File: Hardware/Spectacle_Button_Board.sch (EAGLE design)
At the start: 50 parts, among them J17 AUDIO-JACK3, J19 FTDI_DEVICE, J20 AUDIO-JACK3, U1 CY8C4146LQI-S422, U2 3.3V/150mA

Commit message: Quick schematic changes, ready for QC review
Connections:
- net GND: now also J17.TIP, J20.TIP; no longer J17.RING2, J20.RING2
- net SCL: now also J17.RING2, J20.RING2; no longer J17.RING1, J20.RING1
- net SDA: now also J17.RING1, J20.RING1; no longer J17.TIP, J20.TIP
- net VIN: now also D5.2; no longer D5.1
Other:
- moved on the sheet: D4, J17, J20
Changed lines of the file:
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@@
 <?xml version="1.0" encoding="utf-8"?>
 <!DOCTYPE eagle SYSTEM "eagle.dtd">
-<eagle version="7.3.0">
+<eagle version="7.6.0">
 <drawing>
 <settings>
@@
 <instance part="C5" gate="G$1" x="17.78" y="109.22"/>
 <instance part="C6" gate="G$1" x="7.62" y="109.22"/>
-<instance part="GND9" gate="1" x="185.42" y="63.5"/>
+<instance part="GND9" gate="1" x="180.34" y="63.5"/>
 <instance part="SUPPLY7" gate="G$1" x="190.5" y="93.98"/>
 <instance part="R3" gate="G$1" x="198.12" y="83.82" rot="R90"/>
@@
 <instance part="R6" gate="G$1" x="226.06" y="162.56" rot="R180"/>
 <instance part="GND15" gate="1" x="38.1" y="132.08"/>
-<instance part="J17" gate="G$1" x="167.64" y="73.66"/>
-<instance part="D4" gate="G$1" x="208.28" y="58.42"/>
+<instance part="J17" gate="G$1" x="167.64" y="73.66" rot="MR180"/>
+<instance part="D4" gate="G$1" x="208.28" y="68.58" rot="MR180"/>
 <instance part="D5" gate="G$1" x="208.28" y="40.64"/>
 <instance part="D6" gate="G$1" x="60.96" y="63.5"/>
@@
 <instance part="SUPPLY13" gate="G$1" x="205.74" y="101.6"/>
 <instance part="SUPPLY14" gate="G$1" x="228.6" y="137.16"/>
-<instance part="J20" gate="G$1" x="167.64" y="53.34"/>
-<instance part="GND21" gate="1" x="185.42" y="43.18"/>
+<instance part="J20" gate="G$1" x="167.64" y="53.34" rot="MR180"/>
+<instance part="GND21" gate="1" x="180.34" y="43.18"/>
 <instance part="LOGO1" gate="G$1" x="127" y="15.24"/>
 <instance part="LOGO2" gate="G$1" x="50.8" y="0"/>
@@
 </segment>
 <segment>
-<pinref part="J17" gate="G$1" pin="RING2"/>
 <pinref part="GND9" gate="1" pin="GND"/>
-<wire x1="172.72" y1="68.58" x2="185.42" y2="68.58" width="0.1524" layer="91"/>
-<wire x1="185.42" y1="68.58" x2="185.42" y2="66.04" width="0.1524" layer="91"/>
+<pinref part="J17" gate="G$1" pin="TIP"/>
+<wire x1="172.72" y1="76.2" x2="180.34" y2="76.2" width="0.1524" layer="91"/>
+<wire x1="180.34" y1="76.2" x2="180.34" y2="66.04" width="0.1524" layer="91"/>
 </segment>
 <segment>
@@
 <wire x1="223.52" y1="45.72" x2="226.06" y2="45.72" width="0.1524" layer="91"/>
 <wire x1="226.06" y1="45.72" x2="226.06" y2="43.18" width="0.1524" layer="91"/>
-<wire x1="226.06" y1="45.72" x2="226.06" y2="63.5" width="0.1524" layer="91"/>
-<junction x="226.06" y="45.72"/>
 <pinref part="D4" gate="G$1" pin="3"/>
 <wire x1="226.06" y1="63.5" x2="223.52" y2="63.5" width="0.1524" layer="91"/>
-</segment>
-<segment>
-<pinref part="J20" gate="G$1" pin="RING2"/>
+<wire x1="226.06" y1="63.5" x2="226.06" y2="45.72" width="0.1524" layer="91"/>
+<junction x="226.06" y="45.72"/>
+</segment>
+<segment>
 <pinref part="GND21" gate="1" pin="GND"/>
-<wire x1="172.72" y1="48.26" x2="185.42" y2="48.26" width="0.1524" layer="91"/>
-<wire x1="185.42" y1="48.26" x2="185.42" y2="45.72" width="0.1524" layer="91"/>
+<pinref part="J20" gate="G$1" pin="TIP"/>
+<wire x1="172.72" y1="55.88" x2="180.34" y2="55.88" width="0.1524" layer="91"/>
+<wire x1="180.34" y1="55.88" x2="180.34" y2="45.72" width="0.1524" layer="91"/>
 </segment>
 </net>
@@
 </segment>
 <segment>
+<pinref part="D5" gate="G$1" pin="2"/>
 <pinref part="SUPPLY7" gate="G$1" pin="VIN"/>
+<wire x1="203.2" y1="43.18" x2="190.5" y2="43.18" width="0.1524" layer="91"/>
+<wire x1="190.5" y1="43.18" x2="190.5" y2="48.26" width="0.1524" layer="91"/>
+<pinref part="J20" gate="G$1" pin="EARTH"/>
+<wire x1="190.5" y1="48.26" x2="190.5" y2="68.58" width="0.1524" layer="91"/>
+<wire x1="190.5" y1="68.58" x2="190.5" y2="93.98" width="0.1524" layer="91"/>
+<wire x1="172.72" y1="48.26" x2="190.5" y2="48.26" width="0.1524" layer="91"/>
+<junction x="190.5" y="48.26"/>
 <pinref part="J17" gate="G$1" pin="EARTH"/>
-<wire x1="190.5" y1="78.74" x2="190.5" y2="93.98" width="0.1524" layer="91"/>
-<wire x1="172.72" y1="78.74" x2="190.5" y2="78.74" width="0.1524" layer="91"/>
-<wire x1="190.5" y1="78.74" x2="195.58" y2="78.74" width="0.1524" layer="91"/>
-<junction x="190.5" y="78.74"/>
-<wire x1="195.58" y1="78.74" x2="195.58" y2="58.42" width="0.1524" layer="91"/>
-<pinref part="D5" gate="G$1" pin="1"/>
-<wire x1="195.58" y1="58.42" x2="195.58" y2="48.26" width="0.1524" layer="91"/>
-<wire x1="195.58" y1="48.26" x2="203.2" y2="48.26" width="0.1524" layer="91"/>
-<pinref part="J20" gate="G$1" pin="EARTH"/>
-<wire x1="172.72" y1="58.42" x2="195.58" y2="58.42" width="0.1524" layer="91"/>
-<junction x="195.58" y="58.42"/>
+<wire x1="172.72" y1="68.58" x2="190.5" y2="68.58" width="0.1524" layer="91"/>
+<junction x="190.5" y="68.58"/>
 </segment>
 </net>
@@
 <net name="SCL" class="0">
 <segment>
-<pinref part="R3" gate="G$1" pin="1"/>
-<wire x1="198.12" y1="78.74" x2="198.12" y2="76.2" width="0.1524" layer="91"/>
-<wire x1="198.12" y1="76.2" x2="190.5" y2="76.2" width="0.1524" layer="91"/>
-<wire x1="190.5" y1="76.2" x2="172.72" y2="76.2" width="0.1524" layer="91"/>
-<wire x1="198.12" y1="76.2" x2="200.66" y2="76.2" width="0.1524" layer="91"/>
-<junction x="198.12" y="76.2"/>
-<label x="215.9" y="76.2" size="1.27" layer="95" xref="yes"/>
-<pinref part="J17" gate="G$1" pin="RING1"/>
-<pinref part="D4" gate="G$1" pin="1"/>
-<wire x1="200.66" y1="76.2" x2="215.9" y2="76.2" width="0.1524" layer="91"/>
-<wire x1="203.2" y1="66.04" x2="200.66" y2="66.04" width="0.1524" layer="91"/>
-<wire x1="200.66" y1="66.04" x2="200.66" y2="76.2" width="0.1524" layer="91"/>
-<junction x="200.66" y="76.2"/>
-<pinref part="J20" gate="G$1" pin="RING1"/>
-<wire x1="172.72" y1="55.88" x2="190.5" y2="55.88" width="0.1524" layer="91"/>
-<wire x1="190.5" y1="55.88" x2="190.5" y2="76.2" width="0.1524" layer="91"/>
-<junction x="190.5" y="76.2"/>
-</segment>
-<segment>
 <pinref part="U1" gate="G0" pin="P1.0"/>
 <wire x1="195.58" y1="177.8" x2="198.12" y2="177.8" width="0.1524" layer="91"/>
 <label x="198.12" y="177.8" size="1.27" layer="95" xref="yes"/>
 </segment>
+<segment>
+<pinref part="D4" gate="G$1" pin="1"/>
+<label x="215.9" y="76.2" size="1.27" layer="95" xref="yes"/>
+<pinref part="J17" gate="G$1" pin="RING2"/>
+<wire x1="172.72" y1="78.74" x2="185.42" y2="78.74" width="0.1524" layer="91"/>
+<wire x1="185.42" y1="78.74" x2="187.96" y2="78.74" width="0.1524" layer="91"/>
+<wire x1="187.96" y1="78.74" x2="187.96" y2="76.2" width="0.1524" layer="91"/>
+<wire x1="187.96" y1="76.2" x2="193.04" y2="76.2" width="0.1524" layer="91"/>
+<wire x1="193.04" y1="76.2" x2="198.12" y2="76.2" width="0.1524" layer="91"/>
+<wire x1="198.12" y1="76.2" x2="215.9" y2="76.2" width="0.1524" layer="91"/>
+<wire x1="203.2" y1="60.96" x2="193.04" y2="60.96" width="0.1524" layer="91"/>
+<wire x1="193.04" y1="60.96" x2="193.04" y2="76.2" width="0.1524" layer="91"/>
+<junction x="193.04" y="76.2"/>
+<pinref part="J20" gate="G$1" pin="RING2"/>
+<wire x1="172.72" y1="58.42" x2="185.42" y2="58.42" width="0.1524" layer="91"/>
+<wire x1="185.42" y1="58.42" x2="185.42" y2="78.74" width="0.1524" layer="91"/>
+<junction x="185.42" y="78.74"/>
+<pinref part="R3" gate="G$1" pin="1"/>
+<wire x1="198.12" y1="78.74" x2="198.12" y2="76.2" width="0.1524" layer="91"/>
+<junction x="198.12" y="76.2"/>
+</segment>
 </net>
 <net name="SDA" class="0">
 <segment>
+<pinref part="D4" gate="G$1" pin="2"/>
+<wire x1="203.2" y1="66.04" x2="195.58" y2="66.04" width="0.1524" layer="91"/>
+<wire x1="187.96" y1="73.66" x2="195.58" y2="73.66" width="0.1524" layer="91"/>
+<label x="215.9" y="73.66" size="1.27" layer="95" xref="yes"/>
+<wire x1="195.58" y1="73.66" x2="213.36" y2="73.66" width="0.1524" layer="91"/>
+<wire x1="213.36" y1="73.66" x2="215.9" y2="73.66" width="0.1524" layer="91"/>
+<wire x1="187.96" y1="73.66" x2="187.96" y2="71.12" width="0.1524" layer="91"/>
+<pinref part="J20" gate="G$1" pin="RING1"/>
+<wire x1="187.96" y1="71.12" x2="187.96" y2="50.8" width="0.1524" layer="91"/>
+<wire x1="187.96" y1="50.8" x2="172.72" y2="50.8" width="0.1524" layer="91"/>
+<wire x1="195.58" y1="66.04" x2="195.58" y2="73.66" width="0.1524" layer="91"/>
+<junction x="195.58" y="73.66"/>
+<pinref part="J17" gate="G$1" pin="RING1"/>
+<wire x1="172.72" y1="71.12" x2="187.96" y2="71.12" width="0.1524" layer="91"/>
+<junction x="187.96" y="71.12"/>
 <pinref part="R4" gate="G$1" pin="1"/>
 <wire x1="213.36" y1="78.74" x2="213.36" y2="73.66" width="0.1524" layer="91"/>
-<wire x1="213.36" y1="73.66" x2="198.12" y2="73.66" width="0.1524" layer="91"/>
-<wire x1="198.12" y1="73.66" x2="193.04" y2="73.66" width="0.1524" layer="91"/>
-<wire x1="193.04" y1="73.66" x2="185.42" y2="73.66" width="0.1524" layer="91"/>
-<wire x1="213.36" y1="73.66" x2="215.9" y2="73.66" width="0.1524" layer="91"/>
 <junction x="213.36" y="73.66"/>
-<label x="215.9" y="73.66" size="1.27" layer="95" xref="yes"/>
-<pinref part="J17" gate="G$1" pin="TIP"/>
-<wire x1="172.72" y1="71.12" x2="185.42" y2="71.12" width="0.1524" layer="91"/>
-<wire x1="185.42" y1="71.12" x2="185.42" y2="73.66" width="0.1524" layer="91"/>
-<pinref part="D4" gate="G$1" pin="2"/>
-<wire x1="203.2" y1="60.96" x2="198.12" y2="60.96" width="0.1524" layer="91"/>
-<wire x1="198.12" y1="60.96" x2="198.12" y2="73.66" width="0.1524" layer="91"/>
-<junction x="198.12" y="73.66"/>
-<pinref part="J20" gate="G$1" pin="TIP"/>
-<wire x1="172.72" y1="50.8" x2="193.04" y2="50.8" width="0.1524" layer="91"/>
-<wire x1="193.04" y1="50.8" x2="193.04" y2="73.66" width="0.1524" layer="91"/>
-<junction x="193.04" y="73.66"/>
-</segment>
-<segment>
+</segment>
+<segment>

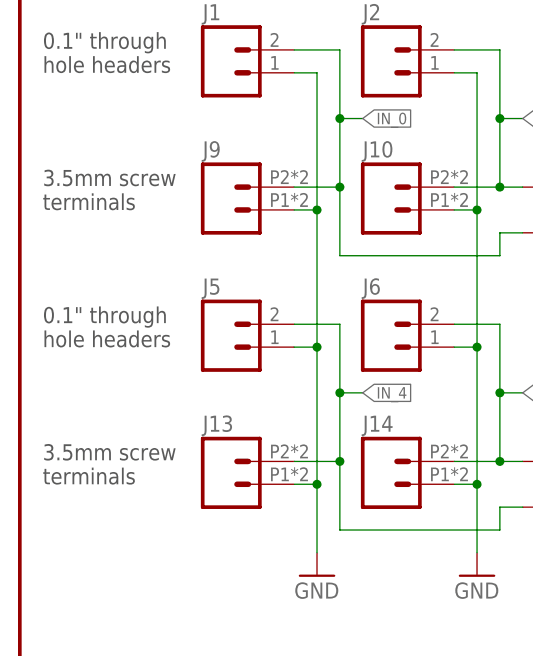
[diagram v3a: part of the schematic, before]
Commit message: Changed text on connectors
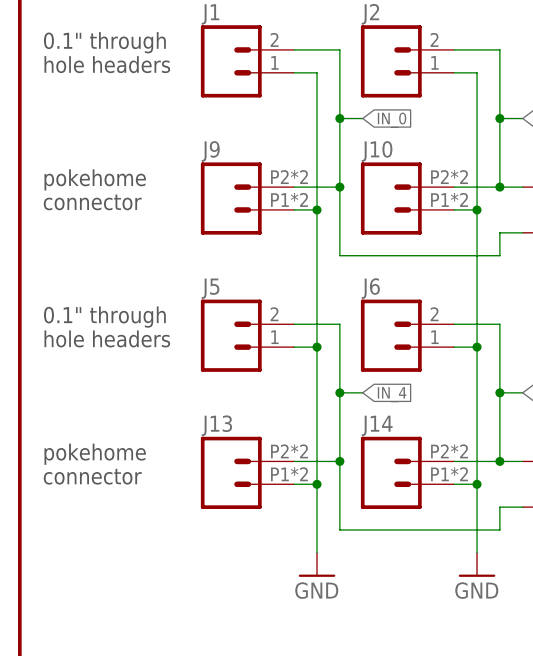
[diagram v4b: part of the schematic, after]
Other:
- note added: "pokehome connector"
- note removed: "3.5mm screw terminals"
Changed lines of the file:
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@@
 <sheet>
 <plain>
-<text x="2.54" y="68.58" size="1.778" layer="97">3.5mm screw
-terminals</text>
-<text x="2.54" y="38.1" size="1.778" layer="97">3.5mm screw
-terminals</text>
+<text x="2.54" y="68.58" size="1.778" layer="97">pokehome
+connector</text>
 <text x="2.54" y="83.82" size="1.778" layer="97">0.1" through
 hole headers</text>
@@
 <text x="238.76" y="7.62" size="2.54" layer="94">01</text>
 <text x="2.794" y="95.758" size="1.778" layer="97">VIN 4-6V</text>
+<text x="2.54" y="38.1" size="1.778" layer="97">pokehome
+connector</text>
 </plain>
 <instances>
